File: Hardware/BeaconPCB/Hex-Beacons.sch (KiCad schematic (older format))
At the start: 0 parts

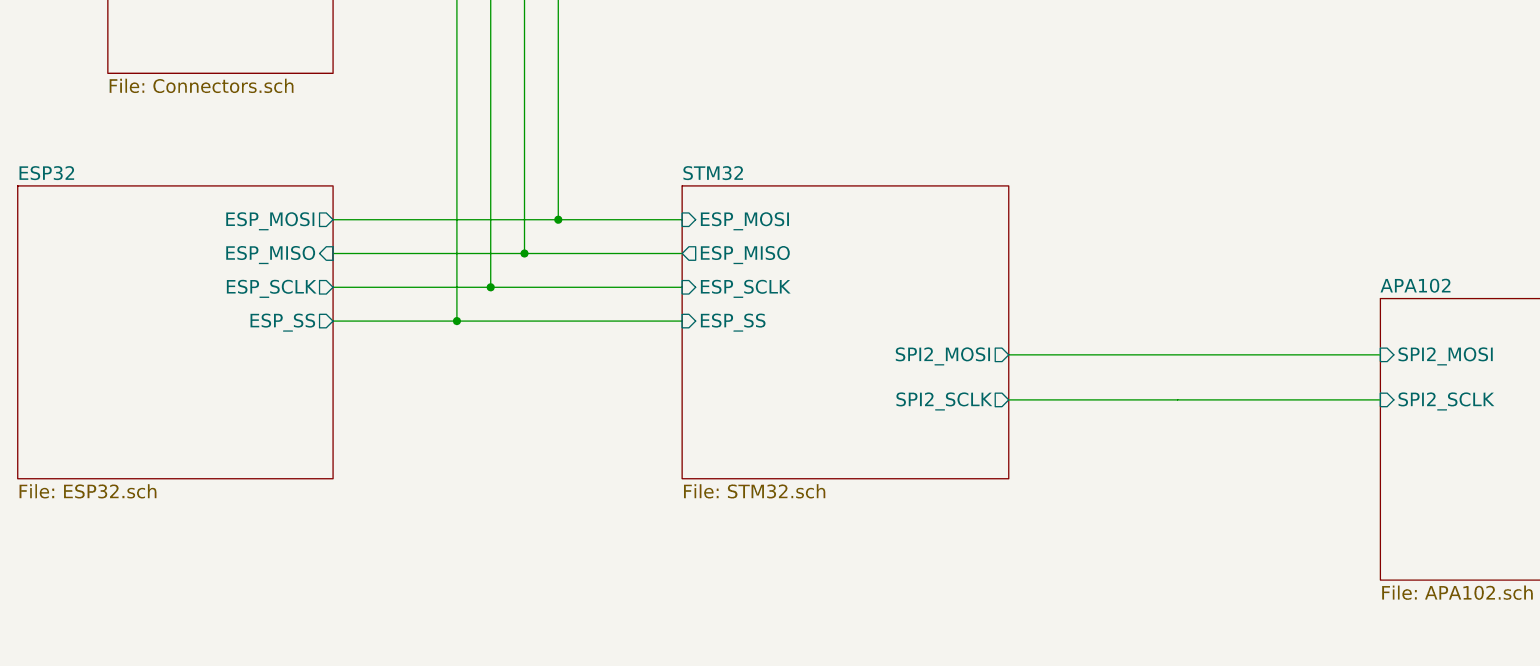
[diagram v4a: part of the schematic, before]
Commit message: Updating Schematic to use Pi Zero W instead of ESP32
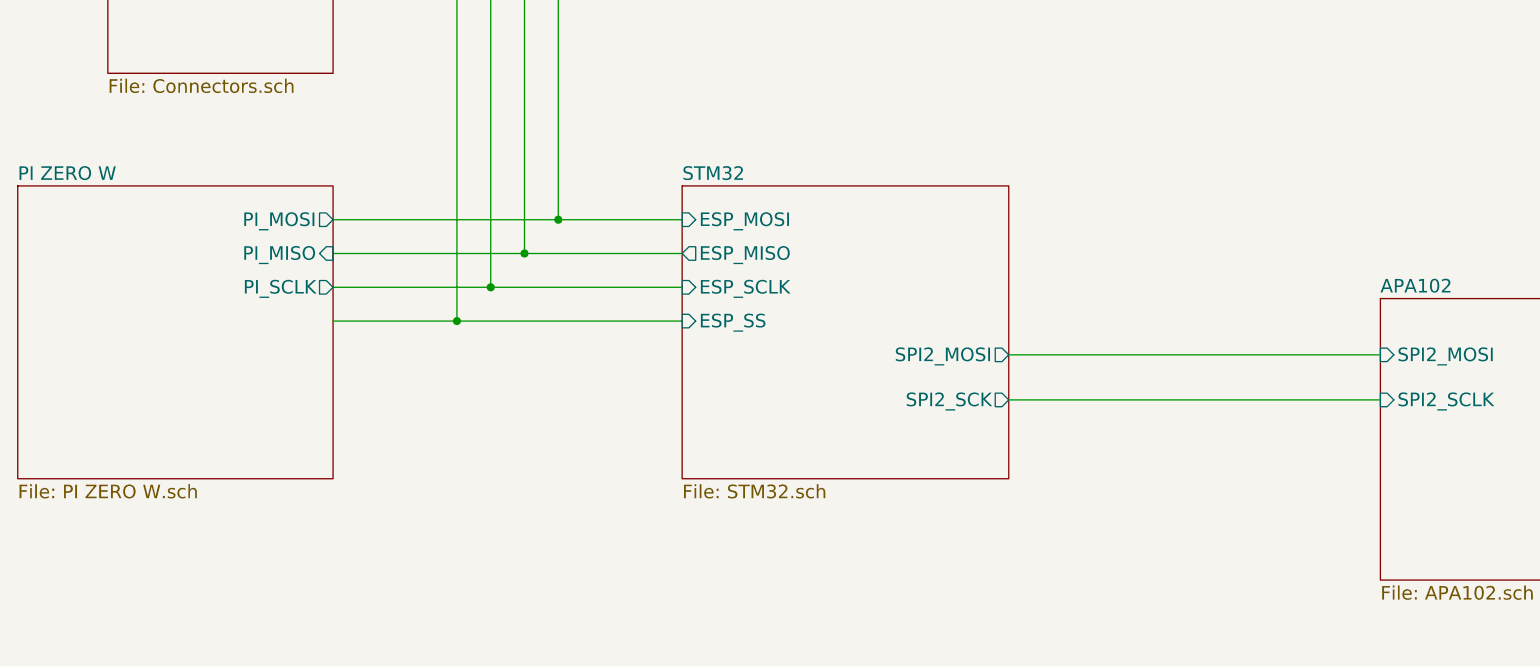
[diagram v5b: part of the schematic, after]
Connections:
- wire segments 20 -> 18
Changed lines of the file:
@@
 S 2150 2450 1400 1300
 U 59AC571E
-F0 "ESP32" 60
-F1 "ESP32.sch" 60
-F2 "ESP_MOSI" O R 3550 2600 60
-F3 "ESP_MISO" I R 3550 2750 60
-F4 "ESP_SCLK" O R 3550 2900 60
-F5 "ESP_SS" O R 3550 3050 60
+F0 "PI ZERO W" 60
+F1 "PI ZERO W.sch" 60
+F2 "PI_MOSI" O R 3550 2600 60
+F3 "PI_MISO" I R 3550 2750 60
+F4 "PI_SCLK" O R 3550 2900 60
 $EndSheet
 $Sheet
@@
 F5 "ESP_MOSI" I L 5100 2600 60
 F6 "SPI2_MOSI" O R 6550 3200 60
-F7 "SPI2_SCLK" O R 6550 3400 60
+F7 "SPI2_SCK" O R 6550 3400 60
 $EndSheet
 $Sheet
@@
 $EndSheet
 Wire Wire Line
-	6550 3400 7300 3400
+	6550 3400 8200 3400
 Wire Wire Line
 	6550 3200 8200 3200
@@
 	4550 1050 4550 2600
 Connection ~ 4550 2600
-Wire Wire Line
-	7300 3400 7300 3400
-Wire Wire Line
-	7300 3400 8200 3400
 $EndSCHEMATC

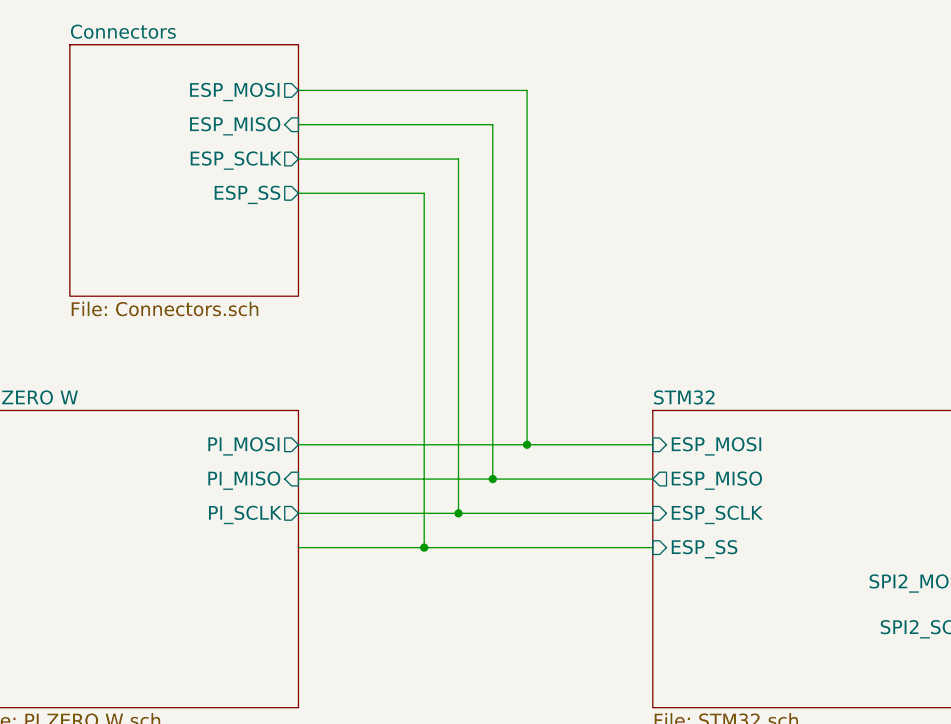
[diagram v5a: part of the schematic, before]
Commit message: Schematic Adjustments
Added 5V power line to Pi header
Adjusted the rest of schematic to use PI SPI lines
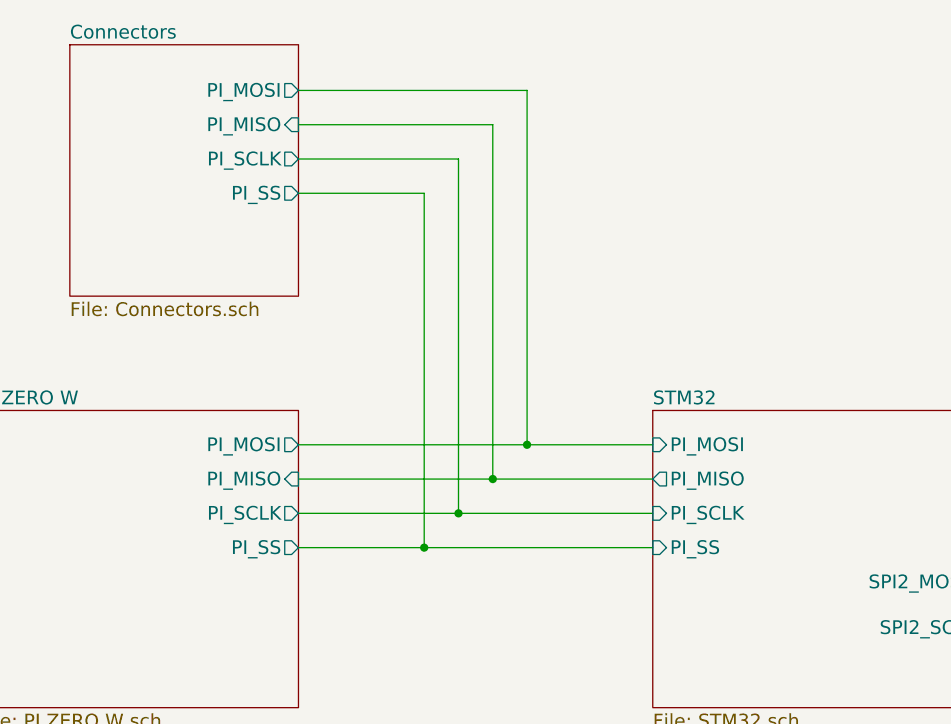
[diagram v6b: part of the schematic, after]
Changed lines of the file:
@@
 F3 "PI_MISO" I R 3550 2750 60
 F4 "PI_SCLK" O R 3550 2900 60
+F5 "PI_SS" O R 3550 3050 60
 $EndSheet
 $Sheet
@@
 F0 "STM32" 60
 F1 "STM32.sch" 60
-F2 "ESP_SS" I L 5100 3050 60
-F3 "ESP_SCLK" I L 5100 2900 60
-F4 "ESP_MISO" O L 5100 2750 60
-F5 "ESP_MOSI" I L 5100 2600 60
-F6 "SPI2_MOSI" O R 6550 3200 60
-F7 "SPI2_SCK" O R 6550 3400 60
+F2 "SPI2_MOSI" O R 6550 3200 60
+F3 "SPI2_SCK" O R 6550 3400 60
+F4 "PI_SS" I L 5100 3050 60
+F5 "PI_SCLK" I L 5100 2900 60
+F6 "PI_MISO" O L 5100 2750 60
+F7 "PI_MOSI" I L 5100 2600 60
 $EndSheet
 $Sheet
@@
 F0 "Connectors" 60
 F1 "Connectors.sch" 60
-F2 "ESP_MOSI" O R 3550 1050 60
-F3 "ESP_MISO" I R 3550 1200 60
-F4 "ESP_SCLK" O R 3550 1350 60
-F5 "ESP_SS" O R 3550 1500 60
+F2 "PI_MOSI" O R 3550 1050 60
+F3 "PI_MISO" I R 3550 1200 60
+F4 "PI_SCLK" O R 3550 1350 60
+F5 "PI_SS" O R 3550 1500 60
 $EndSheet
 Wire Wire Line
